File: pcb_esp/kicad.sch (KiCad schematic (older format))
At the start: 25 parts, among them J1 Prog Pads, J2 SLP, J3 SHT21, J4 BH1750, M1 TP4056Module, SW1 RST, SW2 PRG, U1 LT1963, U2 ESP-12F

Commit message: WIP first board for ESP and regulator
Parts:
- removed BT1: 18650, Battery:BatteryHolder_MPD_BH-18650-PC2, symbol Device:Battery_Cell
- removed M1: TP4056Module, footprints:TP4056_Module, symbol projectlib:TP4056Module
- added J5: PWRIN, Connector_Wire:SolderWirePad_1x01_Drill1mm, symbol Connector_Generic:Conn_01x01
- added J6: GND, Connector_Wire:SolderWirePad_1x01_Drill1mm, symbol Connector_Generic:Conn_01x01
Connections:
- net GND: now also J6.1 (Pin_1); no longer J2.1 (Pin_1), U2.4 (GPIO16)
- net at C2.1, R3.1, U1.5 (~SHDN)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: now also J5.1 (Pin_1)
- new net: J2.1 (Pin_1), U2.4 (GPIO16)
- no-connect marks 13 -> 11
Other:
- moved on the sheet: C1, C2, C3, R1, R2, R3, R4, U1
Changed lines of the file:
@@
 L lt1763:LT1963 U1
 U 1 1 5D66AE48
-P 4350 1100
-F 0 "U1" H 4350 1567 50  0000 C CNN
-F 1 "LT1963" H 4350 1476 50  0000 C CNN
-F 2 "Package_SO:SO-8_3.9x4.9mm_P1.27mm" H 4350 350 50  0001 C CNN
-F 3 "https://www.analog.com/media/en/technical-documentation/data-sheets/1763fh.pdf" H 4350 550 50  0001 C CNN
-	1    4350 1100
+P 4450 1100
+F 0 "U1" H 4450 1567 50  0000 C CNN
+F 1 "LT1963" H 4450 1476 50  0000 C CNN
+F 2 "Package_SO:SO-8_3.9x4.9mm_P1.27mm" H 4450 350 50  0001 C CNN
+F 3 "https://www.analog.com/media/en/technical-documentation/data-sheets/1763fh.pdf" H 4450 550 50  0001 C CNN
+	1    4450 1100
 	1    0    0    -1
 $EndComp
@@
 L Device:C C1
 U 1 1 5D66BDA0
-P 5100 1050
-F 0 "C1" H 5215 1096 50  0000 L CNN
-F 1 "0.01u" H 5215 1005 50  0000 L CNN
-F 2 "Capacitor_SMD:C_1206_3216Metric_Pad1.42x1.75mm_HandSolder" H 5138 900 50  0001 C CNN
-F 3 "~" H 5100 1050 50  0001 C CNN
-	1    5100 1050
-	1    0    0    -1
-$EndComp
-Wire Wire Line
-	4750 900  5100 900
-Wire Wire Line
-	4750 1200 5100 1200
-Wire Wire Line
-	3900 900  3900 1100
-Wire Wire Line
-	3900 1100 3950 1100
-Connection ~ 3900 900
-Wire Wire Line
-	3900 900  3950 900
-Wire Wire Line
-	4250 1400 4350 1400
+P 5200 1050
+F 0 "C1" H 5315 1096 50  0000 L CNN
+F 1 "0.01u" H 5315 1005 50  0000 L CNN
+F 2 "Capacitor_SMD:C_1206_3216Metric_Pad1.42x1.75mm_HandSolder" H 5238 900 50  0001 C CNN
+F 3 "~" H 5200 1050 50  0001 C CNN
+	1    5200 1050
+	1    0    0    -1
+$EndComp
+Wire Wire Line
+	4850 900  5200 900
+Wire Wire Line
+	4850 1200 5200 1200
+Wire Wire Line
+	4000 900  4000 1100
+Wire Wire Line
+	4000 1100 4050 1100
+Connection ~ 4000 900
+Wire Wire Line
+	4000 900  4050 900
 Wire Wire Line
 	4350 1400 4450 1400
-Connection ~ 4350 1400
+Wire Wire Line
+	4450 1400 4550 1400
+Connection ~ 4450 1400
 $Comp
 L Device:R R1
 U 1 1 5D66D87C
-P 5600 1050
-F 0 "R1" H 5670 1096 50  0000 L CNN
-F 1 "1M" H 5670 1005 50  0000 L CNN
-F 2 "Resistor_SMD:R_1206_3216Metric" V 5530 1050 50  0001 C CNN
-F 3 "~" H 5600 1050 50  0001 C CNN
-	1    5600 1050
+P 5700 1050
+F 0 "R1" H 5770 1096 50  0000 L CNN
+F 1 "1M" H 5770 1005 50  0000 L CNN
+F 2 "Resistor_SMD:R_1206_3216Metric" V 5630 1050 50  0001 C CNN
+F 3 "~" H 5700 1050 50  0001 C CNN
+	1    5700 1050
 	1    0    0    -1
 $EndComp
@@
 L Device:R R2
 U 1 1 5D66DD1B
-P 5600 1400
-F 0 "R2" H 5670 1446 50  0000 L CNN
-F 1 "680k" H 5670 1355 50  0000 L CNN
-F 2 "Resistor_SMD:R_1206_3216Metric" V 5530 1400 50  0001 C CNN
-F 3 "~" H 5600 1400 50  0001 C CNN
-	1    5600 1400
-	1    0    0    -1
-$EndComp
-Wire Wire Line
-	5100 900  5600 900
-Connection ~ 5100 900
-Wire Wire Line
-	4750 1000 4950 1000
-Wire Wire Line
-	4950 1000 4950 1250
-Wire Wire Line
-	4950 1250 5600 1250
-Wire Wire Line
-	5600 1250 5600 1200
-Connection ~ 5600 1250
-Wire Wire Line
-	5600 1550 4450 1550
-Wire Wire Line
-	4450 1550 4450 1400
-Connection ~ 4450 1400
+P 5700 1400
+F 0 "R2" H 5770 1446 50  0000 L CNN
+F 1 "680k" H 5770 1355 50  0000 L CNN
+F 2 "Resistor_SMD:R_1206_3216Metric" V 5630 1400 50  0001 C CNN
+F 3 "~" H 5700 1400 50  0001 C CNN
+	1    5700 1400
+	1    0    0    -1
+$EndComp
+Wire Wire Line
+	5200 900  5700 900
+Connection ~ 5200 900
+Wire Wire Line
+	4850 1000 5050 1000
+Wire Wire Line
+	5050 1000 5050 1250
+Wire Wire Line
+	5050 1250 5700 1250
+Wire Wire Line
+	5700 1250 5700 1200
+Connection ~ 5700 1250
+Wire Wire Line
+	5700 1550 4550 1550
+Wire Wire Line
+	4550 1550 4550 1400
+Connection ~ 4550 1400
 $Comp
 L Device:CP C3
 U 1 1 5D66F7C0
-P 6100 1200
-F 0 "C3" H 6218 1246 50  0000 L CNN
-F 1 "10u" H 6218 1155 50  0000 L CNN
-F 2 "Capacitor_THT:CP_Radial_D5.0mm_P2.50mm" H 6138 1050 50  0001 C CNN
-F 3 "~" H 6100 1200 50  0001 C CNN
-	1    6100 1200
-	1    0    0    -1
-$EndComp
-Wire Wire Line
-	5600 900  6100 900
-Wire Wire Line
-	6100 900  6100 1050
-Connection ~ 5600 900
-Wire Wire Line
-	5600 1550 6100 1550
-Wire Wire Line
-	6100 1550 6100 1350
-Connection ~ 5600 1550
+P 6200 1200
+F 0 "C3" H 6318 1246 50  0000 L CNN
+F 1 "10u" H 6318 1155 50  0000 L CNN
+F 2 "Capacitor_THT:CP_Radial_D5.0mm_P2.50mm" H 6238 1050 50  0001 C CNN
+F 3 "~" H 6200 1200 50  0001 C CNN
+	1    6200 1200
+	1    0    0    -1
+$EndComp
+Wire Wire Line
+	5700 900  6200 900
+Wire Wire Line
+	6200 900  6200 1050
+Connection ~ 5700 900
+Wire Wire Line
+	5700 1550 6200 1550
+Wire Wire Line
+	6200 1550 6200 1350
+Connection ~ 5700 1550
 $Comp
 L Device:CP C2
 U 1 1 5D66CA68
-P 3100 1050
-F 0 "C2" H 3218 1096 50  0000 L CNN
-F 1 "10u" H 3218 1005 50  0000 L CNN
-F 2 "Capacitor_THT:CP_Radial_D5.0mm_P2.50mm" H 3138 900 50  0001 C CNN
-F 3 "~" H 3100 1050 50  0001 C CNN
-	1    3100 1050
-	1    0    0    -1
-$EndComp
-Wire Wire Line
-	3100 900  3550 900
+P 3200 1050
+F 0 "C2" H 3318 1096 50  0000 L CNN
+F 1 "10u" H 3318 1005 50  0000 L CNN
+F 2 "Capacitor_THT:CP_Radial_D5.0mm_P2.50mm" H 3238 900 50  0001 C CNN
+F 3 "~" H 3200 1050 50  0001 C CNN
+	1    3200 1050
+	1    0    0    -1
+$EndComp
+Wire Wire Line
+	3200 900  3650 900
 $Comp
 L Device:R R3
 U 1 1 5D68000D
-P 3550 1050
-F 0 "R3" H 3620 1096 50  0000 L CNN
-F 1 "1M" H 3620 1005 50  0000 L CNN
-F 2 "Resistor_SMD:R_1206_3216Metric" V 3480 1050 50  0001 C CNN
-F 3 "~" H 3550 1050 50  0001 C CNN
-	1    3550 1050
-	1    0    0    -1
-$EndComp
-Connection ~ 3550 900
-Wire Wire Line
-	3550 900  3900 900
+P 3650 1050
+F 0 "R3" H 3720 1096 50  0000 L CNN
+F 1 "1M" H 3720 1005 50  0000 L CNN
+F 2 "Resistor_SMD:R_1206_3216Metric" V 3580 1050 50  0001 C CNN
+F 3 "~" H 3650 1050 50  0001 C CNN
+	1    3650 1050
+	1    0    0    -1
+$EndComp
+Connection ~ 3650 900
+Wire Wire Line
+	3650 900  4000 900
 $Comp
 L Device:R R4
 U 1 1 5D68063C
-P 3550 1400
-F 0 "R4" H 3620 1446 50  0000 L CNN
-F 1 "220k" H 3620 1355 50  0000 L CNN
-F 2 "Resistor_SMD:R_1206_3216Metric" V 3480 1400 50  0001 C CNN
-F 3 "~" H 3550 1400 50  0001 C CNN
-	1    3550 1400
-	1    0    0    -1
-$EndComp
-Wire Wire Line
-	4250 1400 4250 1550
-Wire Wire Line
-	4250 1550 3550 1550
-Connection ~ 4250 1400
-Connection ~ 3550 1550
-Wire Wire Line
-	3100 1200 3100 1550
-Wire Wire Line
-	3550 1200 3550 1250
-Text GLabel 3450 1200 0    50   Output ~ 0
+P 3650 1400
+F 0 "R4" H 3720 1446 50  0000 L CNN
+F 1 "220k" H 3720 1355 50  0000 L CNN
+F 2 "Resistor_SMD:R_1206_3216Metric" V 3580 1400 50  0001 C CNN
+F 3 "~" H 3650 1400 50  0001 C CNN
+	1    3650 1400
+	1    0    0    -1
+$EndComp
+Wire Wire Line
+	4350 1400 4350 1550
+Wire Wire Line
+	4350 1550 3650 1550
+Connection ~ 4350 1400
+Connection ~ 3650 1550
+Wire Wire Line
+	3200 1200 3200 1550
+Wire Wire Line
+	3650 1200 3650 1250
+Text GLabel 3550 1200 0    50   Output ~ 0
 ADC
 Wire Wire Line
-	3450 1200 3550 1200
-Connection ~ 3550 1200
-$Comp
-L projectlib:TP4056Module M1
-U 1 1 5D68A11D
-P 1350 1000
-F 0 "M1" H 1375 1365 50  0000 C CNN
-F 1 "TP4056Module" H 1375 1274 50  0000 C CNN
-F 2 "footprints:TP4056_Module" H 1350 1000 50  0001 C CNN
-F 3 "" H 1350 1000 50  0001 C CNN
-	1    1350 1000
-	1    0    0    -1
-$EndComp
-Wire Wire Line
-	1950 900  3100 900
-Connection ~ 3100 900
-Wire Wire Line
-	1950 1100 2550 1100
-Wire Wire Line
-	2550 1100 2550 1550
-Wire Wire Line
-	2550 1550 3100 1550
-Connection ~ 3100 1550
-Wire Wire Line
-	3100 1550 3550 1550
-$Comp
-L Device:Battery_Cell BT1
-U 1 1 5D6973D2
-P 1400 2000
-F 0 "BT1" V 1655 2050 50  0000 C CNN
-F 1 "18650" V 1250 2050 50  0000 C CNN
-F 2 "Battery:BatteryHolder_MPD_BH-18650-PC2" V 1400 2060 50  0001 C CNN
-F 3 "~" V 1400 2060 50  0001 C CNN
-	1    1400 2000
-	0    -1   -1   0
-$EndComp
-Wire Wire Line
-	1200 2000 1200 1300
-Wire Wire Line
-	1200 1300 1250 1300
-Wire Wire Line
-	1500 1300 1500 2000
-Text GLabel 6250 900  2    50   Output ~ 0
+	3550 1200 3650 1200
+Connection ~ 3650 1200
+Wire Wire Line
+	3200 1550 3650 1550
+Text GLabel 6350 900  2    50   Output ~ 0
 PWR
-Text GLabel 6250 1550 2    50   Output ~ 0
+Text GLabel 6350 1550 2    50   Output ~ 0
 GND
 Wire Wire Line
-	6250 1550 6100 1550
-Connection ~ 6100 1550
-Wire Wire Line
-	6250 900  6100 900
-Connection ~ 6100 900
+	6350 1550 6200 1550
+Connection ~ 6200 1550
+Wire Wire Line
+	6350 900  6200 900
+Connection ~ 6200 900
 Text GLabel 1350 2450 0    50   Input ~ 0
 PWR
@@
 Wire Wire Line
 	4850 3300 5000 3300
-NoConn ~ 800  900
-NoConn ~ 800  1100
 Wire Wire Line
 	1950 4200 2800 4200
@@
 	3300 3950 3300 4100
 Wire Wire Line
-	3300 4100 4250 4100
-Wire Wire Line
 	4850 4100 4850 3800
-Connection ~ 4250 4100
-Wire Wire Line
-	4250 4100 4850 4100
 Wire Wire Line
 	3300 3450 3300 3300
@@
 Wire Wire Line
 	2900 5300 3250 5300
+$Comp
+L Connector_Generic:Conn_01x01 J5
+U 1 1 5D74DF00
+P 2450 900
+F 0 "J5" H 2368 675 50  0000 C CNN
+F 1 "PWRIN" H 2368 766 50  0000 C CNN
+F 2 "Connector_Wire:SolderWirePad_1x01_Drill1mm" H 2450 900 50  0001 C CNN
+F 3 "~" H 2450 900 50  0001 C CNN
+	1    2450 900
+	-1   0    0    1
+$EndComp
+$Comp
+L Connector_Generic:Conn_01x01 J6
+U 1 1 5D74E42F
+P 2450 1550
+F 0 "J6" H 2368 1325 50  0000 C CNN
+F 1 "GND" H 2368 1416 50  0000 C CNN
+F 2 "Connector_Wire:SolderWirePad_1x01_Drill1mm" H 2450 1550 50  0001 C CNN
+F 3 "~" H 2450 1550 50  0001 C CNN
+	1    2450 1550
+	-1   0    0    1
+$EndComp
+Wire Wire Line
+	2650 900  3200 900
+Connection ~ 3200 900
+Wire Wire Line
+	2650 1550 3200 1550
+Connection ~ 3200 1550
+Wire Wire Line
+	3300 4100 4850 4100
 $EndSCHEMATC

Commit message: Edge layer for to pcb, making it smaller (30 wide)
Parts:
- C4: footprint Capacitor_SMD:C_1206_3216Metric -> Capacitor_SMD:C_1206_3216Metric_Pad1.42x1.75mm_HandSolder
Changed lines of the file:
@@
 F 0 "C4" H 1615 3396 50  0000 L CNN
 F 1 "0.01u" H 1615 3305 50  0000 L CNN
-F 2 "Capacitor_SMD:C_1206_3216Metric" H 1538 3200 50  0001 C CNN
+F 2 "Capacitor_SMD:C_1206_3216Metric_Pad1.42x1.75mm_HandSolder" H 1538 3200 50  0001 C CNN
 F 3 "~" H 1500 3350 50  0001 C CNN
 	1    1500 3350

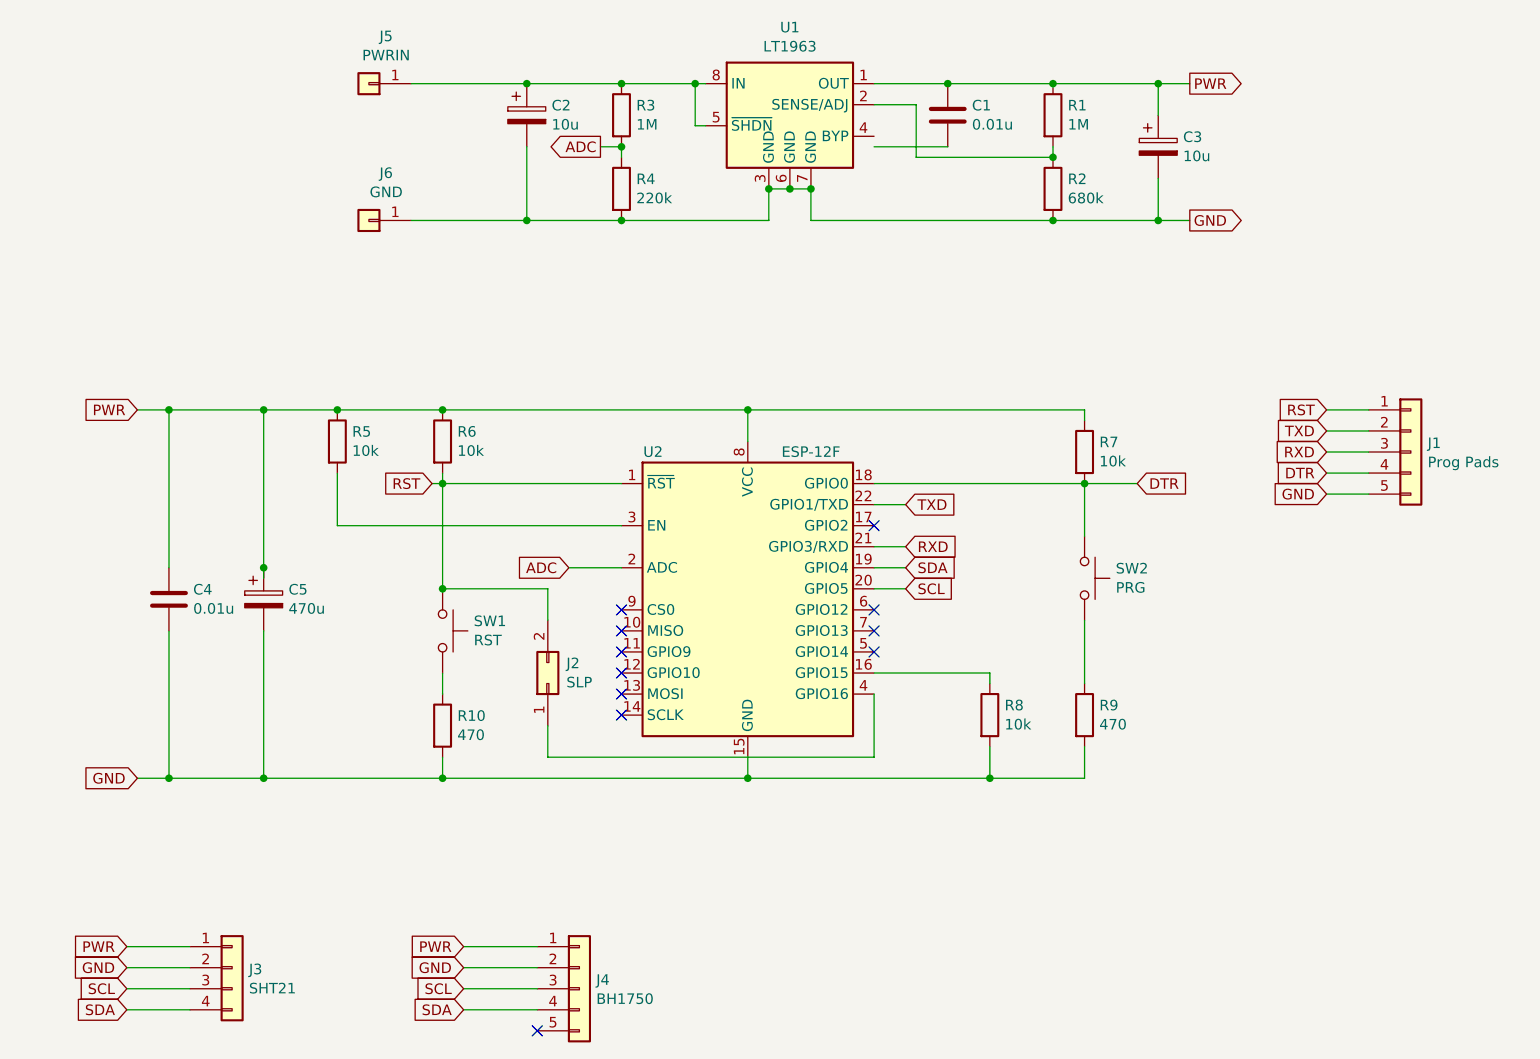
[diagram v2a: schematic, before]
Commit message: ESP module - placed and connected
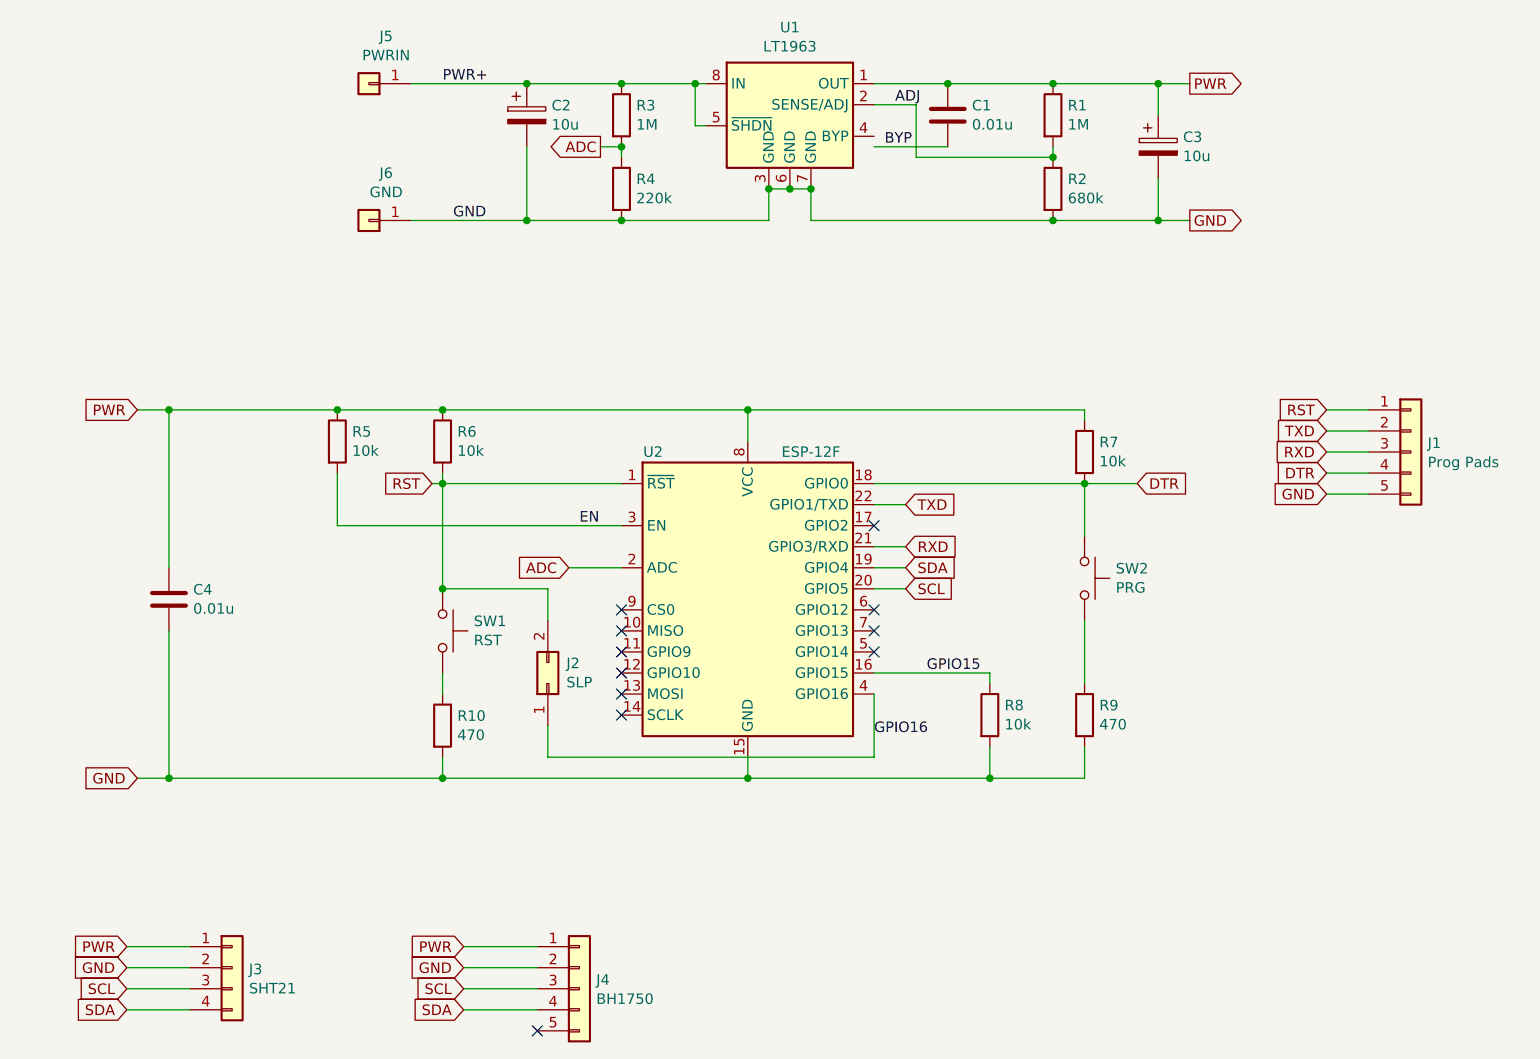
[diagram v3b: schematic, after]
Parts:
- removed C5: 470u, Capacitor_THT:CP_Radial_D5.0mm_P2.50mm, symbol Device:CP
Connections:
- net ADJ: now reaches R1.2, R2.1, U1.2 (SENSE/ADJ)
- net PWR+: now reaches C2.1, J5.1 (Pin_1), R3.1, U1.5 (~SHDN), U1.8 (IN)
- net BYP: now reaches C1.2
- net GPIO15: now reaches R8.1, U2.16 (GPIO15)
- net EN: now reaches R5.2, U2.3 (EN)
- net GPIO16: now reaches J2.1 (Pin_1), U2.4 (GPIO16)
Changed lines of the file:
@@
 Connection ~ 5400 4200
-$Comp
-L Device:CP C5
-U 1 1 5D6DCA12
-P 1950 3350
-F 0 "C5" H 2068 3396 50  0000 L CNN
-F 1 "470u" H 2068 3305 50  0000 L CNN
-F 2 "Capacitor_THT:CP_Radial_D5.0mm_P2.50mm" H 1988 3200 50  0001 C CNN
-F 3 "~" H 1950 3350 50  0001 C CNN
-	1    1950 3350
-	1    0    0    -1
-$EndComp
 $Comp
 L Device:C C4
@@
 	1500 3200 1500 2450
 Connection ~ 1500 2450
-Wire Wire Line
-	1950 3250 1950 3200
-Wire Wire Line
-	1500 2450 1950 2450
-Connection ~ 1950 2450
-Wire Wire Line
-	1950 2450 2300 2450
-Connection ~ 1950 3200
-Wire Wire Line
-	1950 3200 1950 2450
-Wire Wire Line
-	1950 3500 1950 4200
-Connection ~ 1950 4200
-Wire Wire Line
-	1950 4200 1500 4200
 Wire Wire Line
 	1500 3500 1500 4200
@@
 	4850 3300 5000 3300
 Wire Wire Line
-	1950 4200 2800 4200
-Wire Wire Line
 	2800 2800 2800 3300
 Connection ~ 2800 2800
@@
 Wire Wire Line
 	3300 4100 4850 4100
+Wire Wire Line
+	1500 4200 2800 4200
+Wire Wire Line
+	1500 2450 2300 2450
+Text Label 2800 900  0    50   ~ 0
+PWR+
+Text Label 2850 1550 0    50   ~ 0
+GND
+Text Label 4850 4000 0    50   ~ 0
+GPIO16
+Text Label 3450 3000 0    50   ~ 0
+EN
+Text Label 5100 3700 0    50   ~ 0
+GPIO15
+Text Label 4950 1000 0    50   ~ 0
+ADJ
+Text Label 4900 1200 0    50   ~ 0
+BYP
 $EndSCHEMATC

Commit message: Change button footprint, ad kicad logo.
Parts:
- SW1, SW2: footprint Button_Switch_SMD:SW_Push_SPST_NO_Alps_SKRK -> Button_Switch_SMD:SW_SPST_SKQG_WithStem
- U1: footprint Package_SO:SO-8_3.9x4.9mm_P1.27mm -> Package_SO:SOIC-8_3.9x4.9mm_P1.27mm
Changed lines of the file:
@@
 F 0 "U1" H 4450 1567 50  0000 C CNN
 F 1 "LT1963" H 4450 1476 50  0000 C CNN
-F 2 "Package_SO:SO-8_3.9x4.9mm_P1.27mm" H 4450 350 50  0001 C CNN
+F 2 "Package_SO:SOIC-8_3.9x4.9mm_P1.27mm" H 4450 350 50  0001 C CNN
 F 3 "https://www.analog.com/media/en/technical-documentation/data-sheets/1763fh.pdf" H 4450 550 50  0001 C CNN
 	1    4450 1100
@@
 F 0 "SW1" V 2754 3648 50  0000 L CNN
 F 1 "RST" V 2845 3648 50  0000 L CNN
-F 2 "Button_Switch_SMD:SW_Push_SPST_NO_Alps_SKRK" H 2800 3700 50  0001 C CNN
+F 2 "Button_Switch_SMD:SW_SPST_SKQG_WithStem" H 2800 3700 50  0001 C CNN
 F 3 "~" H 2800 3700 50  0001 C CNN
 	1    2800 3500
@@
 F 0 "SW2" V 5804 3398 50  0000 L CNN
 F 1 "PRG" V 5895 3398 50  0000 L CNN
-F 2 "Button_Switch_SMD:SW_Push_SPST_NO_Alps_SKRK" H 5850 3450 50  0001 C CNN
+F 2 "Button_Switch_SMD:SW_SPST_SKQG_WithStem" H 5850 3450 50  0001 C CNN
 F 3 "~" H 5850 3450 50  0001 C CNN
 	1    5850 3250

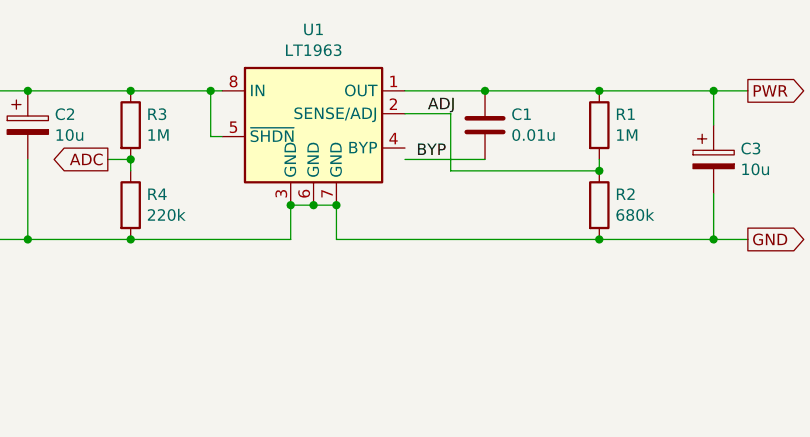
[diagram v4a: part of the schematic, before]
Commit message: Fix lt1763 symbol (swapped gnd and byp pins) and fix pcb
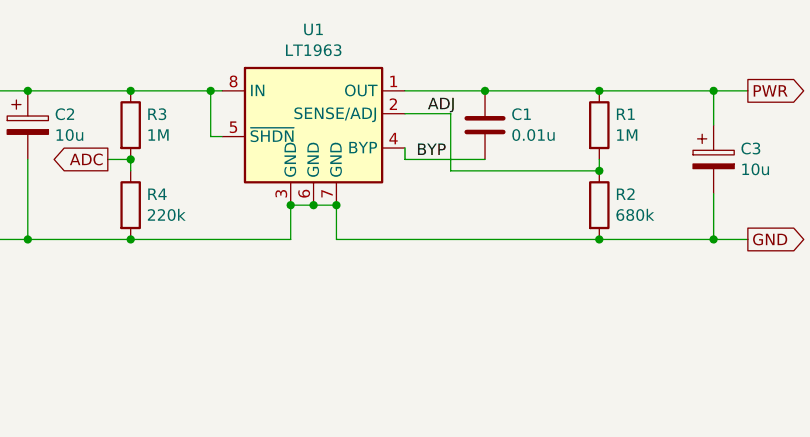
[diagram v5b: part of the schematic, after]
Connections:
- net BYP: now also U1.4 (BYP)
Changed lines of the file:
@@
 	4850 900  5200 900
-Wire Wire Line
-	4850 1200 5200 1200
 Wire Wire Line
 	4000 900  4000 1100
@@
 Text Label 4900 1200 0    50   ~ 0
 BYP
+Wire Wire Line
+	4850 1150 4850 1200
+Wire Wire Line
+	4850 1200 5200 1200
 $EndSCHEMATC
